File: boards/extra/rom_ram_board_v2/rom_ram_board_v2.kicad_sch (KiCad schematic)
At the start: 23 parts, among them J1 Exp. Conn. A, J2 Exp. Conn. B, J3 Power, J4 Exp. Conn. C, J5 BANK SELECT, U1 74LS139, U2 SST39SF040, U3 AS6C4008-55PCN, U4 AS6C4008-55PCN, U5 AS6C4008-55PCN

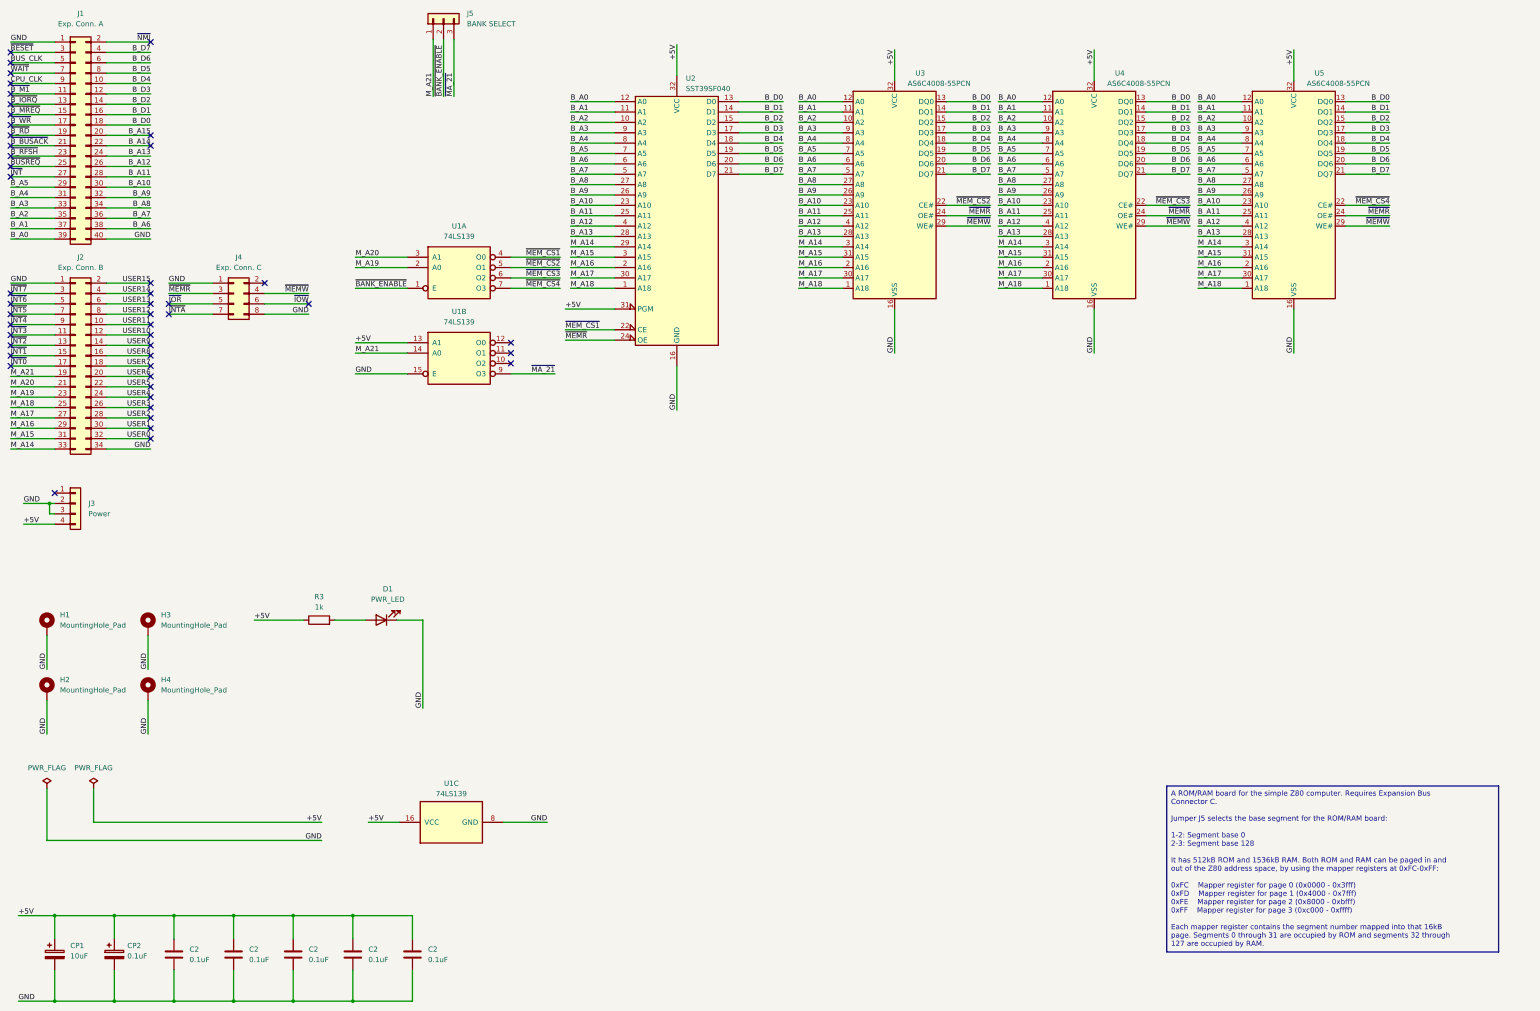
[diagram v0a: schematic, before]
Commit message: Updated ROM/RAM Board V2
Updated the ROM/RAM Board V2 to revision 1.1
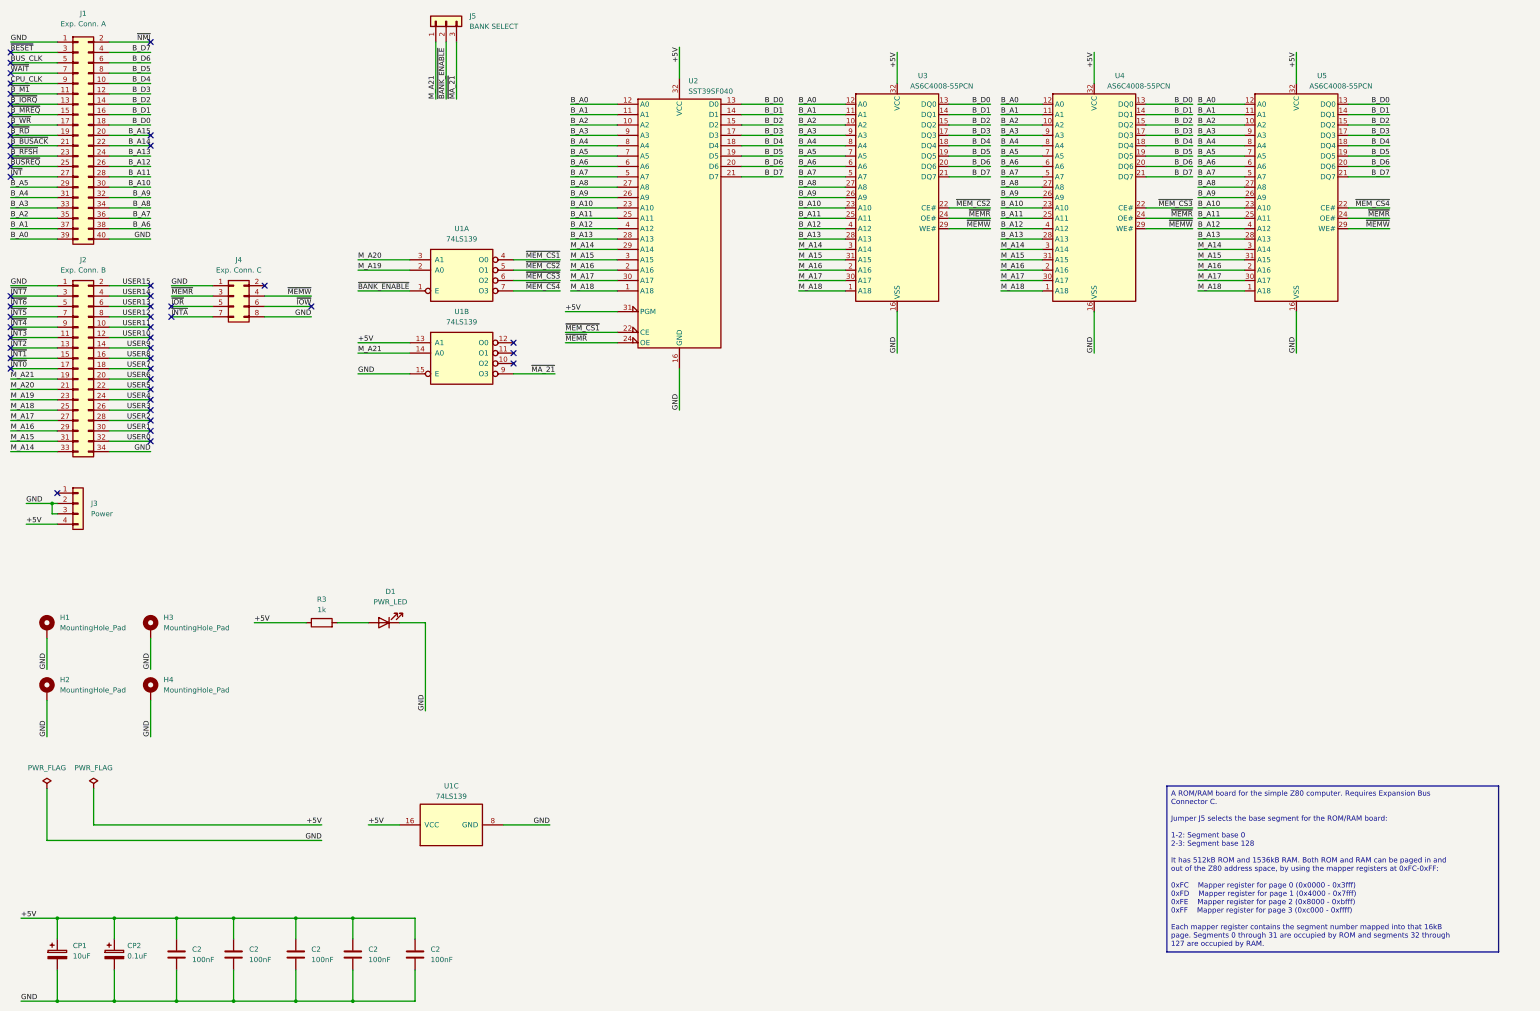
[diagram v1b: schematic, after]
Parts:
- C2: value 0.1uF -> 100nF; MPN (none) -> 178MU0006; Manufacturer (none) -> KNSCHA; Package (none) -> Plugin,P=2.54mm
- CP1: MPN (none) -> ECA1HM100I; Manufacturer (none) -> PANASONIC; Package (none) -> Plugin,D5xL11mm
- CP2: MPN (none) -> KS104M050C07RR0VH2FP0; Manufacturer (none) -> CX(Dongguan Chengxing Elec); Package (none) -> Plugin,D4xL7mm
- D1: MPN (none) -> HLMP-1700; Manufacturer (none) -> Broadcom/AVAGO; Package (none) -> LED_D3.0mm
- H1, H2, H3, H4: now left out of the parts list
- J1: MPN (none) -> X9555WR-2x20-6TV01; Manufacturer (none) -> XKB Connectivity; Package (none) -> Push-Pull,P=2.54mm
- J2: MPN (none) -> X9555WR-2x17-6TV01; Manufacturer (none) -> XKB Connectivity; Package (none) -> Push-Pull,P=2.54mm
- J3: MPN (none) -> 171826-4; Manufacturer (none) -> TE Connectivity AMP Connectors; Package (none) -> Plugin
- J4: MPN (none) -> 75867-132LF; Manufacturer (none) -> Amphenol ICC; Package (none) -> Push-Pull,P=2.54mm
- J5: MPN (none) -> PZ254R-11-03P; Manufacturer (none) -> XFCN; Package (none) -> Push-Pull,P=2.54mm
- R3: MPN (none) -> MBA02040C1001FC100; Manufacturer (none) -> Vishay Intertech; Package (none) -> Plugin
- U1: MPN (none) -> IC-16P; Manufacturer (none) -> BOOMELE(Boom Precision Elec); Package (none) -> DIP-16
- U2, U3, U4, U5: MPN (none) -> Z-ICS0S32P-WG00; Manufacturer (none) -> Ckmtw(Shenzhen Cankemeng); Package (none) -> DIP-32
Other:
- moved on the sheet: C2, CP1, D1, H1, H3, H4, J1, J2, J3, J4, J5, R3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
